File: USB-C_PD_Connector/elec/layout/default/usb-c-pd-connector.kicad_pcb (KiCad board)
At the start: 2 copper layers, 20 x 20 mm, 0 parts

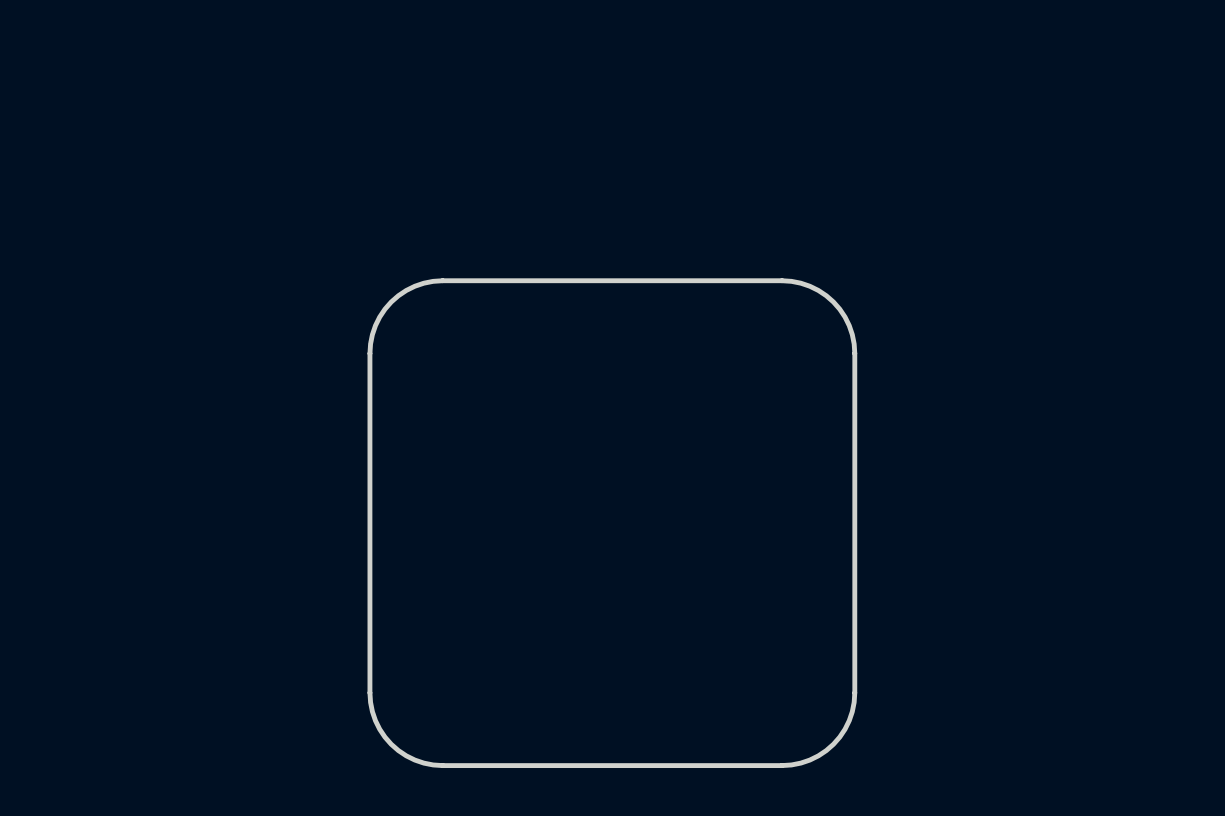
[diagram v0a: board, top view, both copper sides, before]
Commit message: completed pcb module for USB-C connector for 100W USB PD
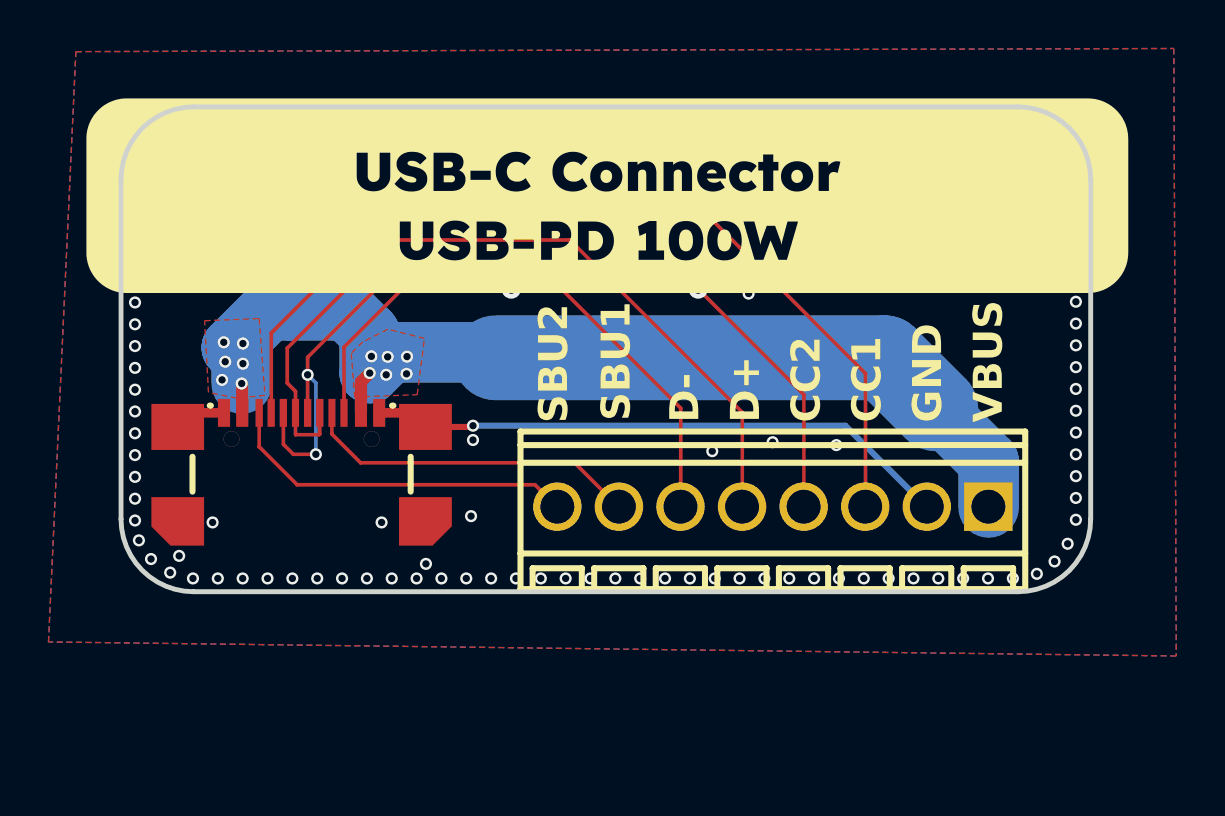
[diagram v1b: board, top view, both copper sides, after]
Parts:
- added REF**: OSHW-Logo_5.7x6mm_SilkScreen, Symbol:OSHW-Logo_5.7x6mm_SilkScreen, B.Cu at (91.0, 60.6)
- added U1: , lib:USB-C-SMD_TYPE-C-31-M-22, F.Cu at (91.2, 65.6)
- added U2: , lib:CONN-TH_XY308-2.54-8P, F.Cu at (110.7, 67.2)
- added U3: , lib:MountingHole_3.2mm_M3, F.Cu at (119.5, 55.0)
- added U4: , lib:MountingHole_3.2mm_M3, F.Cu at (88.0, 55.0)
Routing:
- net vbus: track 0.00 -> 42.3 mm, vias 0 -> 12
- net cc1: track 0.00 -> 38.1 mm
- net dp: track 0.00 -> 33.1 mm
- net dm: track 0.00 -> 32.1 mm, vias 0 -> 2
- net cc2: track 0.00 -> 29.2 mm, vias 0 -> 2
- net gnd: track 0.00 -> 26.4 mm, vias 0 -> 157
- net sbu2: track 0.00 -> 14.7 mm
- net sbu1: track 0.00 -> 14.0 mm
- added copper zone on B.Cu, net gnd
- added copper zone on F.Cu, net gnd
- added copper zone on F.Cu, net vbus
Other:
- board size 20 x 20 mm -> 40 x 20 mm
- board text added: "CC1"
- board text added: "CC2"
- board text added: "D+"
- board text added: "D-"
- board text added: "GND"
- board text added: "SBU1"
- board text added: "SBU2"
- board text added: "Source files:"
- board text added: "VBUS"
- board text added: "bit.ly/44GNFXk"
- board text added: "{{GITHASH}}"
